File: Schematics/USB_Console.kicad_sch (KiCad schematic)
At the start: 8 parts, among them IC2 TPD2EUSB30ADRTR, IC3 CP2102N-A02-GQFN24R, J24 1051330011

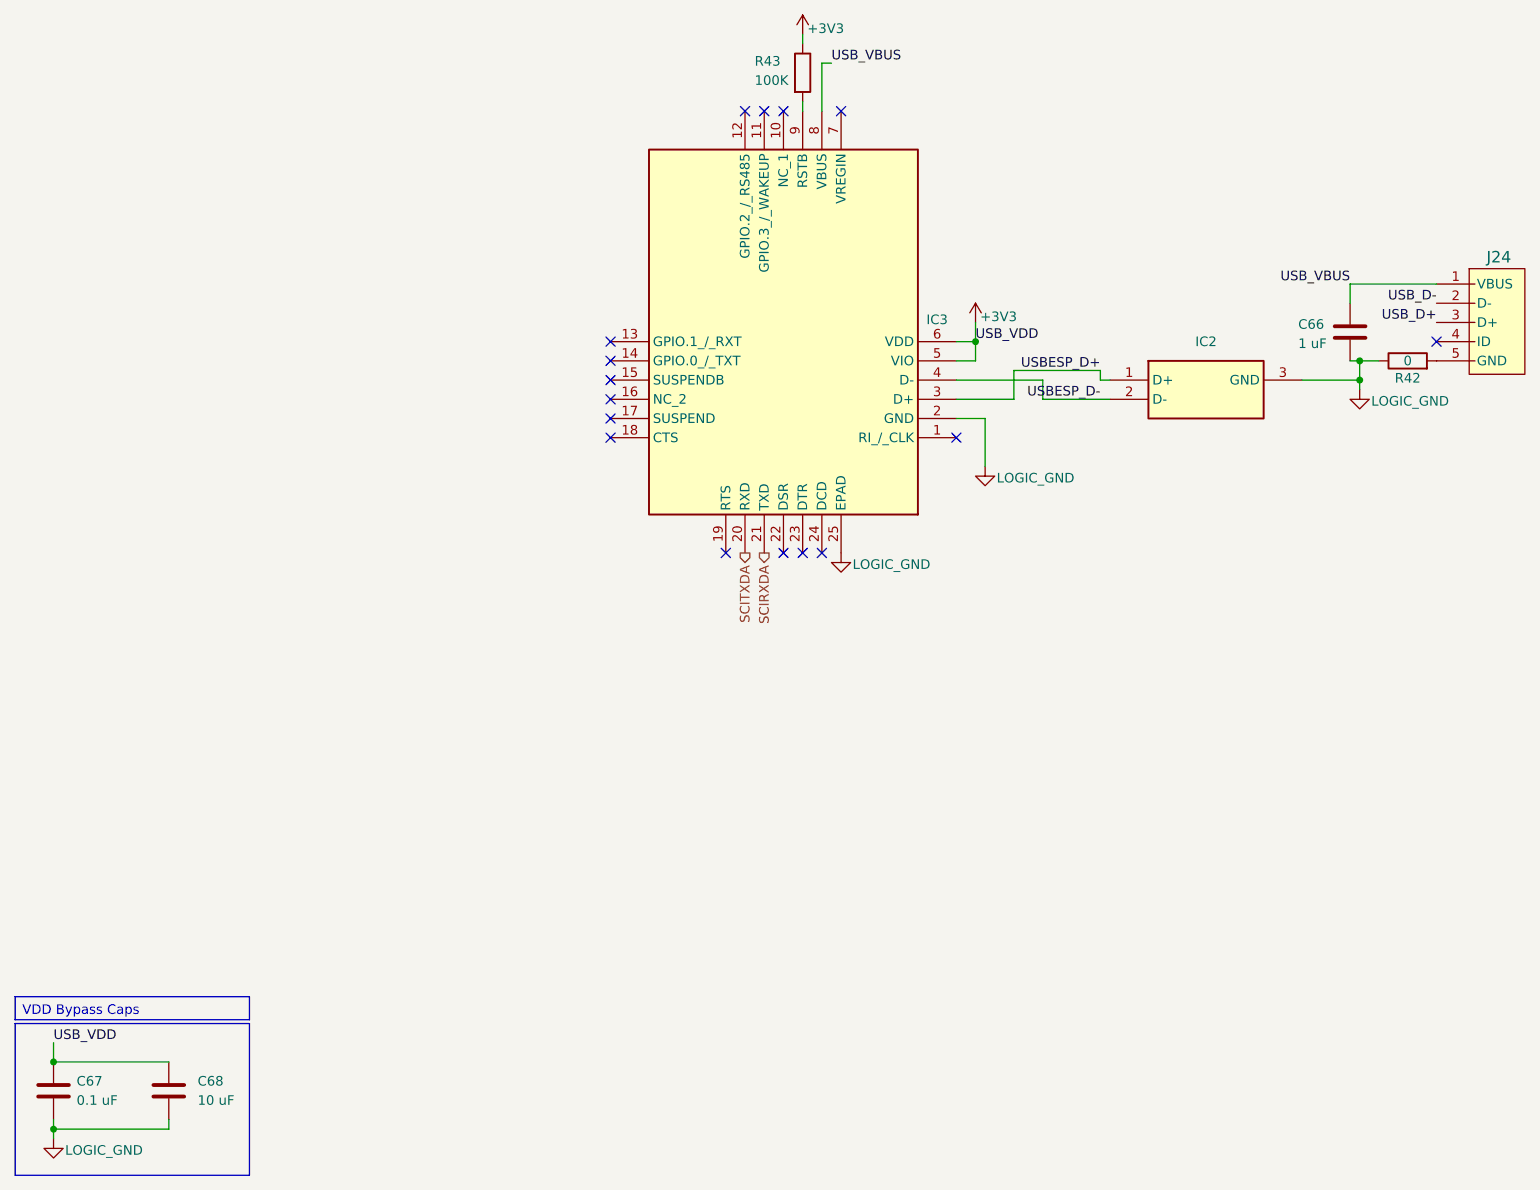
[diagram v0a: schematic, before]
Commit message: [Milestone Compelted Controller and USB]
- Added Test Points
- Completed USB circuit to Controller
- Wired up Controller
- Added Connectors to Power Subsheet and 12pin from cotnroller to Full
  Bridge
- Added 3d models for USB compoents
- General fixes to subsheets
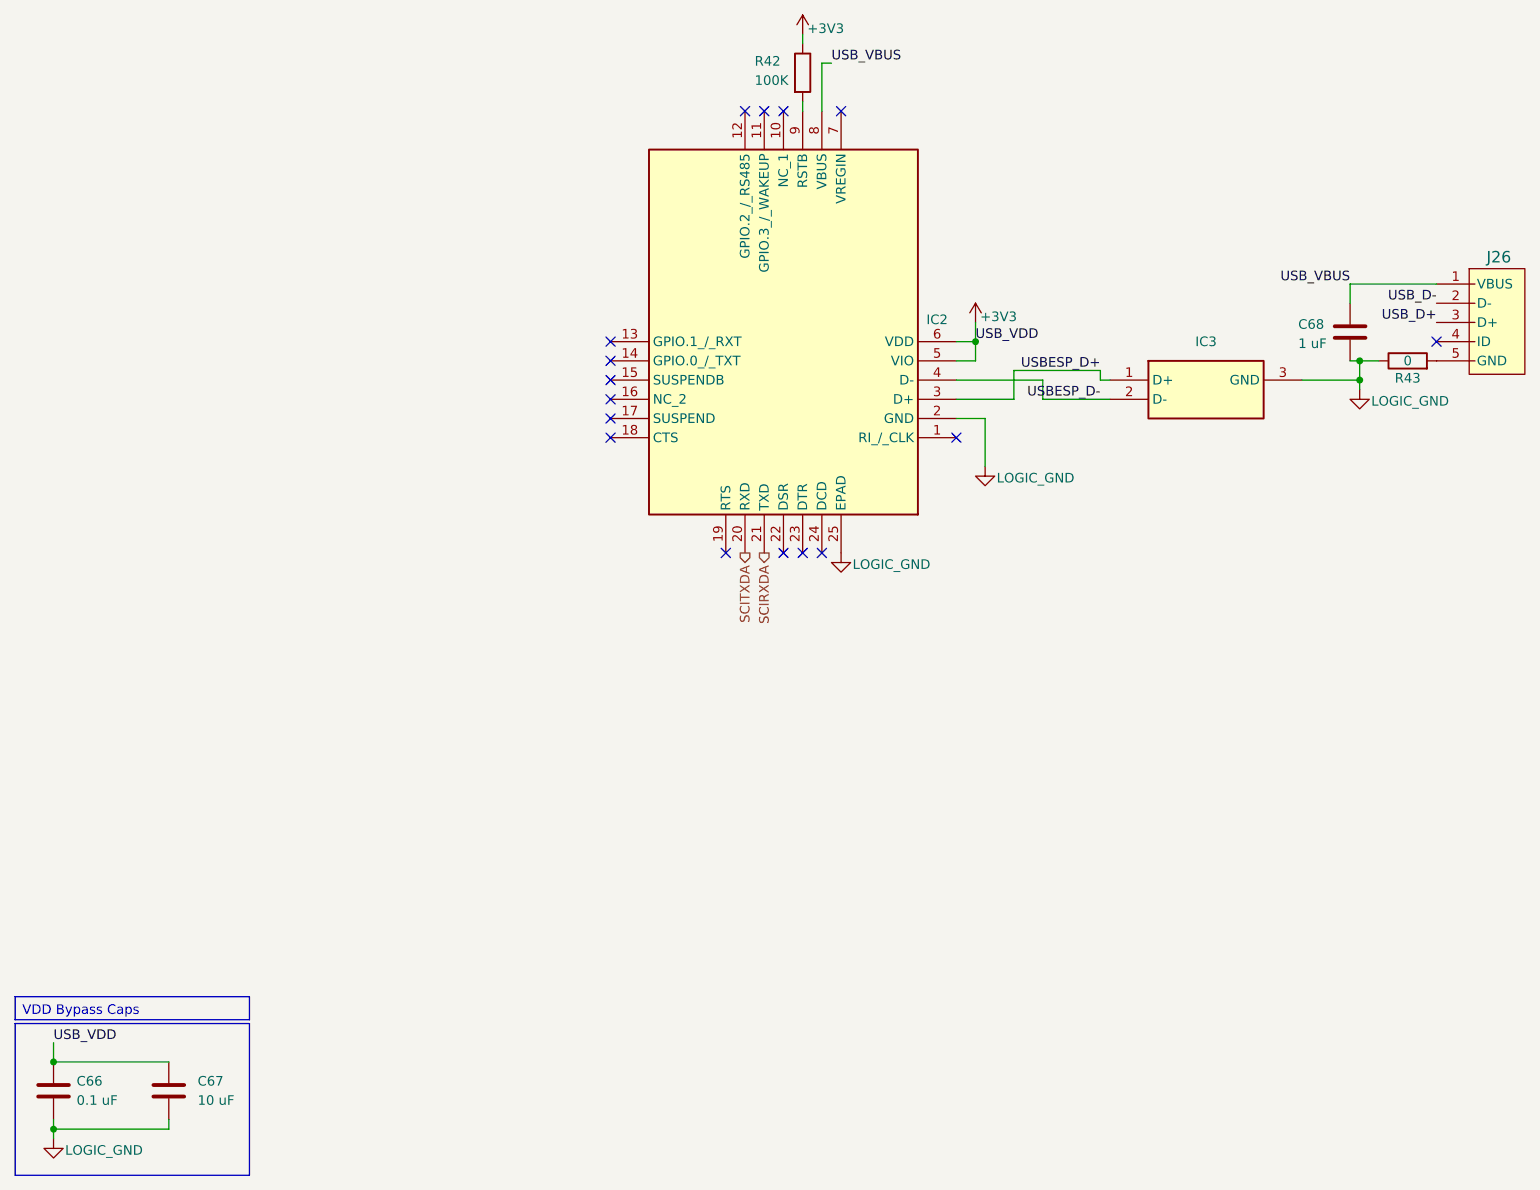
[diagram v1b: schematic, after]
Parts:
- renumbered C67 to C66, C68 to C67, C66 to C68, IC3 to IC2, IC2 to IC3, J24 to J26, R43 to R42, R42 to R43

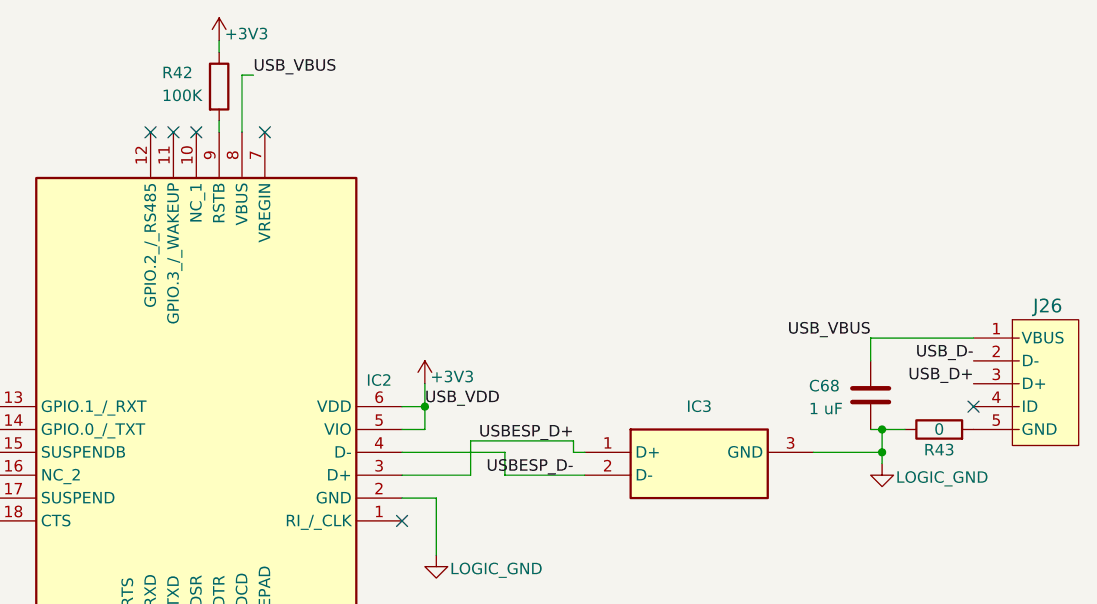
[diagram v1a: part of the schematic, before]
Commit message: [WIP Input Protection Circuit to Controller]
- Added Gate node input protection pin to controller
- Added optocoupler to input protection circuit
- Added 3d model for PC817.....
- Updated PCB to test out PCB modularity
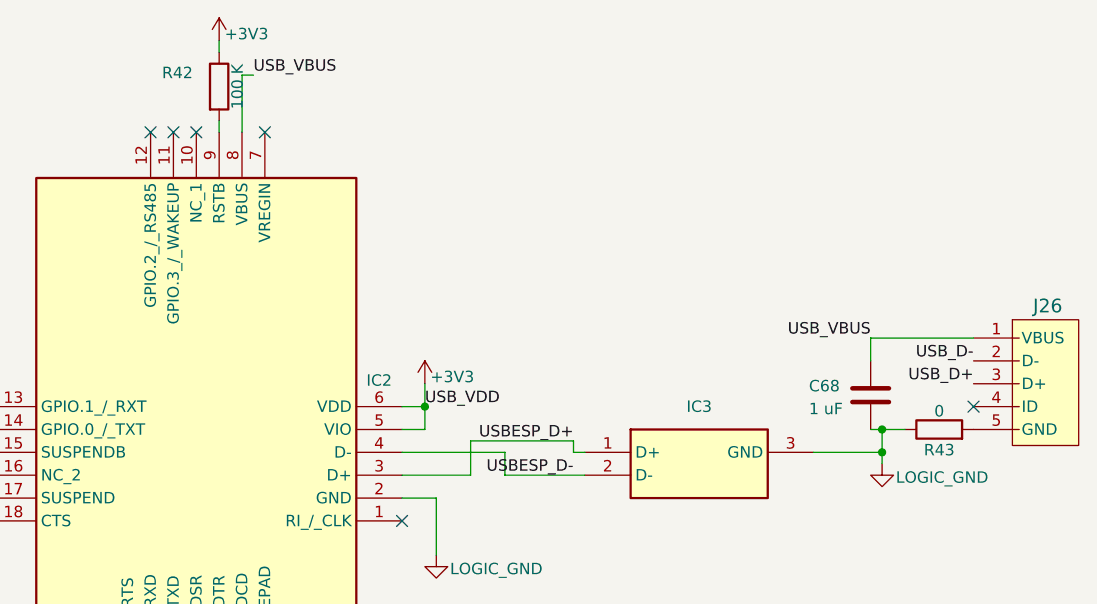
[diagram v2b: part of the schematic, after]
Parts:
- R42: value 100K -> 100 K; symbol Device:R -> SiC_Inverter:RT1206BRD07100KL
- R43: symbol Device:R -> SiC_Inverter:MCA12060Z0000ZP500
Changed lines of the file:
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@@
 	)
 	(symbol
-		(lib_id "Device:R")
+		(lib_id "SiC_Inverter:RT1206BRD07100KL")
 		(at 123.19 44.45 0)
 		(unit 1)
@@
 			)
 		)
-		(property "Value" "100K"
-			(at 116.84 45.466 0)
-			(effects
-				(font
-					(size 1.27 1.27)
-				)
-				(justify left)
+		(property "Value" "100 K"
+			(at 125.222 44.45 90)
+			(effects
+				(font
+					(size 1.27 1.27)
+				)
 			)
 		)
 		(property "Footprint" "Resistor_SMD:R_1206_3216Metric_Pad1.30x1.75mm_HandSolder"
-			(at 121.412 44.45 90)
-			(effects
-				(font
-					(size 1.27 1.27)
-				)
-				(hide yes)
-			)
-		)
-		(property "Datasheet" "~"
-			(at 123.19 44.45 0)
-			(effects
-				(font
-					(size 1.27 1.27)
-				)
-				(hide yes)
-			)
-		)
-		(property "Description" "Resistor"
-			(at 123.19 44.45 0)
+			(at 136.144 55.88 0)
+			(effects
+				(font
+					(size 1.27 1.27)
+				)
+				(hide yes)
+			)
+		)
+		(property "Datasheet" "https://www.mouser.com/datasheet/3/508/1/PYu-RT_1-to-0.01_RoHS_L_15.pdf"
+			(at 145.542 58.166 0)
+			(effects
+				(font
+					(size 1.27 1.27)
+				)
+				(hide yes)
+			)
+		)
+		(property "Description" "Thin Film Resistors - SMD 1/4W 5K ohm .1% 25ppm"
+			(at 131.826 60.452 0)
 			(effects
 				(font
@@
 	)
 	(symbol
-		(lib_id "Device:R")
+		(lib_id "SiC_Inverter:MCA12060Z0000ZP500")
 		(at 203.2 82.55 90)
 		(unit 1)
@@
 		)
 		(property "Value" "0"
-			(at 203.2 82.55 90)
+			(at 203.2 80.518 90)
 			(effects
 				(font
@@
 		)
 		(property "Footprint" "Resistor_SMD:R_1206_3216Metric_Pad1.30x1.75mm_HandSolder"
-			(at 203.2 84.328 90)
-			(effects
-				(font
-					(size 1.27 1.27)
-				)
-				(hide yes)
-			)
-		)
-		(property "Datasheet" "~"
-			(at 203.2 82.55 0)
-			(effects
-				(font
-					(size 1.27 1.27)
-				)
-				(hide yes)
-			)
-		)
-		(property "Description" "Resistor"
-			(at 203.2 82.55 0)
-			(effects
-				(font
+			(at 214.63 69.596 0)
+			(effects
+				(font
+					(size 1.27 1.27)
+				)
+				(hide yes)
+			)
+		)
+		(property "Datasheet" "https://www.vishay.com/docs/28705/mcx0x0xpro.pdf"
+			(at 216.916 60.198 0)
+			(effects
+				(font
+					(size 1.27 1.27)
+				)
+				(hide yes)
+			)
+		)
+		(property "Description" "Thin Film Resistors - SMD MCA 1206 P5 0R0"
+			(at 219.202 73.914 0)
+			(effects
+				(font

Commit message: WIP PCB, Added Test Points, added icon file
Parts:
- renumbered C66 to C67, C67 to C68, C68 to C69, J26 to J28, R42 to R48, R43 to R49
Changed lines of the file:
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@@
 		(on_board yes)
 		(dnp no)
-		(property "Reference" "#PWR0138"
+		(property "Reference" "#PWR0147"
 			(at 146.05 81.28 0)
 			(effects
@@
 			(project "SiC_Single_Phase_Inverter"
 				(path "/a1ed0539-9735-4ad1-a8fd-87e26e7fce16/a4e77945-709f-47b6-8253-e2d18e80adc4"
-					(reference "#PWR0138")
+					(reference "#PWR0147")
 					(unit 1)
 				)
@@
 		(on_board yes)
 		(dnp no)
-		(property "Reference" "J26"
+		(property "Reference" "J28"
 			(at 213.614 68.834 0)
 			(effects
@@
 			(project "SiC_Single_Phase_Inverter"
 				(path "/a1ed0539-9735-4ad1-a8fd-87e26e7fce16/a4e77945-709f-47b6-8253-e2d18e80adc4"
-					(reference "J26")
+					(reference "J28")
 					(unit 1)
 				)
@@
 		(on_board yes)
 		(dnp no)
-		(property "Reference" "C66"
+		(property "Reference" "C67"
 			(at 27.178 177.8 0)
 			(effects
@@
 			(project "SiC_Single_Phase_Inverter"
 				(path "/a1ed0539-9735-4ad1-a8fd-87e26e7fce16/a4e77945-709f-47b6-8253-e2d18e80adc4"
-					(reference "C66")
+					(reference "C67")
 					(unit 1)
 				)
@@
 		(on_board yes)
 		(dnp no)
-		(property "Reference" "#PWR0136"
+		(property "Reference" "#PWR0145"
 			(at 123.19 43.18 0)
 			(effects
@@
 			(project "SiC_Single_Phase_Inverter"
 				(path "/a1ed0539-9735-4ad1-a8fd-87e26e7fce16/a4e77945-709f-47b6-8253-e2d18e80adc4"
-					(reference "#PWR0136")
+					(reference "#PWR0145")
 					(unit 1)
 				)
@@
 		(on_board yes)
 		(dnp no)
-		(property "Reference" "#PWR0137"
+		(property "Reference" "#PWR0146"
 			(at 128.27 114.3 0)
 			(effects
@@
 			(project "SiC_Single_Phase_Inverter"
 				(path "/a1ed0539-9735-4ad1-a8fd-87e26e7fce16/a4e77945-709f-47b6-8253-e2d18e80adc4"
-					(reference "#PWR0137")
+					(reference "#PWR0146")
 					(unit 1)
 				)
@@
 		(on_board yes)
 		(dnp no)
-		(property "Reference" "R42"
+		(property "Reference" "R48"
 			(at 116.84 42.926 0)
 			(effects
@@
 			(project "SiC_Single_Phase_Inverter"
 				(path "/a1ed0539-9735-4ad1-a8fd-87e26e7fce16/a4e77945-709f-47b6-8253-e2d18e80adc4"
-					(reference "R42")
+					(reference "R48")
 					(unit 1)
 				)
@@
 		(on_board yes)
 		(dnp no)
-		(property "Reference" "#PWR0139"
+		(property "Reference" "#PWR0148"
 			(at 147.32 102.87 0)
 			(effects
@@
 			(project "SiC_Single_Phase_Inverter"
 				(path "/a1ed0539-9735-4ad1-a8fd-87e26e7fce16/a4e77945-709f-47b6-8253-e2d18e80adc4"
-					(reference "#PWR0139")
+					(reference "#PWR0148")
 					(unit 1)
 				)
@@
 		(dnp no)
 		(fields_autoplaced yes)
-		(property "Reference" "C67"
+		(property "Reference" "C68"
 			(at 43.18 177.7999 0)
 			(effects
@@
 			(project ""
 				(path "/a1ed0539-9735-4ad1-a8fd-87e26e7fce16/a4e77945-709f-47b6-8253-e2d18e80adc4"
-					(reference "C67")
+					(reference "C68")
 					(unit 1)
 				)
@@
 		(on_board yes)
 		(dnp no)
-		(property "Reference" "#PWR0135"
+		(property "Reference" "#PWR0144"
 			(at 24.13 191.77 0)
 			(effects
@@
 			(project "SiC_Single_Phase_Inverter"
 				(path "/a1ed0539-9735-4ad1-a8fd-87e26e7fce16/a4e77945-709f-47b6-8253-e2d18e80adc4"
-					(reference "#PWR0135")
+					(reference "#PWR0144")
 					(unit 1)
 				)
@@
 		(on_board yes)
 		(dnp no)
-		(property "Reference" "R43"
+		(property "Reference" "R49"
 			(at 203.2 84.836 90)
 			(effects
@@
 			(project "SiC_Single_Phase_Inverter"
 				(path "/a1ed0539-9735-4ad1-a8fd-87e26e7fce16/a4e77945-709f-47b6-8253-e2d18e80adc4"
-					(reference "R43")
+					(reference "R49")
 					(unit 1)
 				)
@@
 		(on_board yes)
 		(dnp no)
-		(property "Reference" "#PWR0140"
+		(property "Reference" "#PWR0149"
 			(at 196.85 92.71 0)
 			(effects
@@
 			(project "SiC_Single_Phase_Inverter"
 				(path "/a1ed0539-9735-4ad1-a8fd-87e26e7fce16/a4e77945-709f-47b6-8253-e2d18e80adc4"
-					(reference "#PWR0140")
+					(reference "#PWR0149")
 					(unit 1)
 				)
@@
 		(on_board yes)
 		(dnp no)
-		(property "Reference" "C68"
+		(property "Reference" "C69"
 			(at 188.722 77.724 0)
 			(effects
@@
 			(project "SiC_Single_Phase_Inverter"
 				(path "/a1ed0539-9735-4ad1-a8fd-87e26e7fce16/a4e77945-709f-47b6-8253-e2d18e80adc4"
-					(reference "C68")
-					(unit 1)
-				)
+					(reference "C69")
+					(unit 1)
+				)

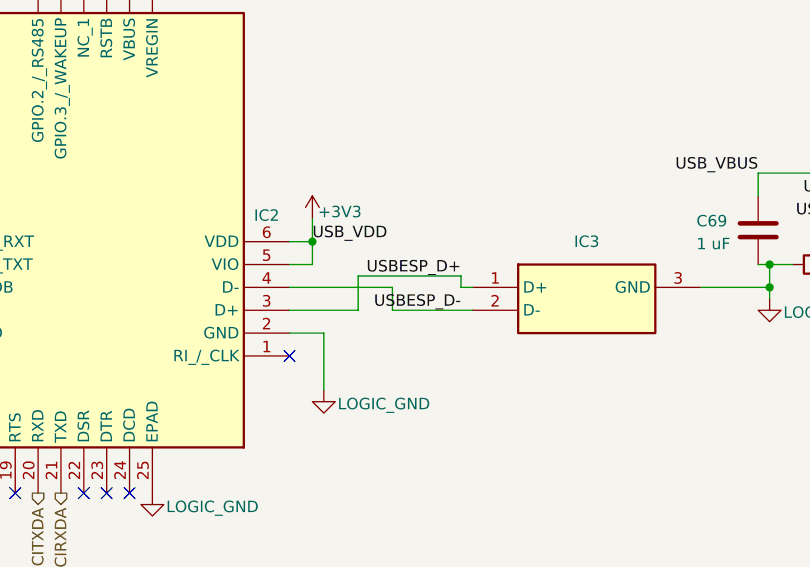
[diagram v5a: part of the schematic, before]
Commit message: WIP PCB Design Controller
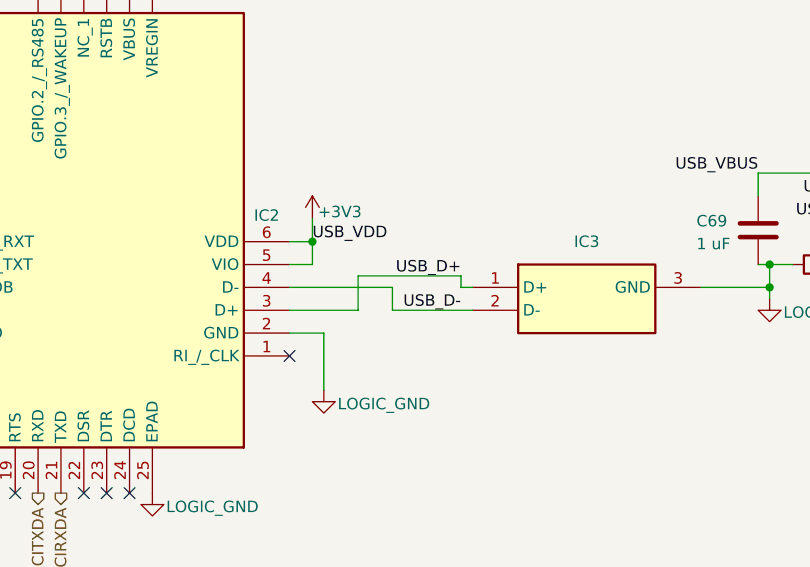
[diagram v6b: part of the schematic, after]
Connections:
- net USBESP_D+ is gone; now on net USB_D+: IC2.3 (D+), IC3.1 (D+)
- net USBESP_D- is gone; now on net USB_D-: IC2.4 (D-), IC3.2 (D-)
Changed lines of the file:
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@@
 		)
 	)
-	(label "USBESP_D-"
+	(label "USB_D-"
 		(at 162.56 87.63 180)
 		(effects
@@
 		)
 	)
-	(label "USBESP_D+"
+	(label "USB_D+"
 		(at 162.56 83.82 180)
 		(effects
